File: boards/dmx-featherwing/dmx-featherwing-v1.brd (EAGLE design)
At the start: 50.8 x 22.9 mm, 4 parts, among them U2 MAX3468CSA

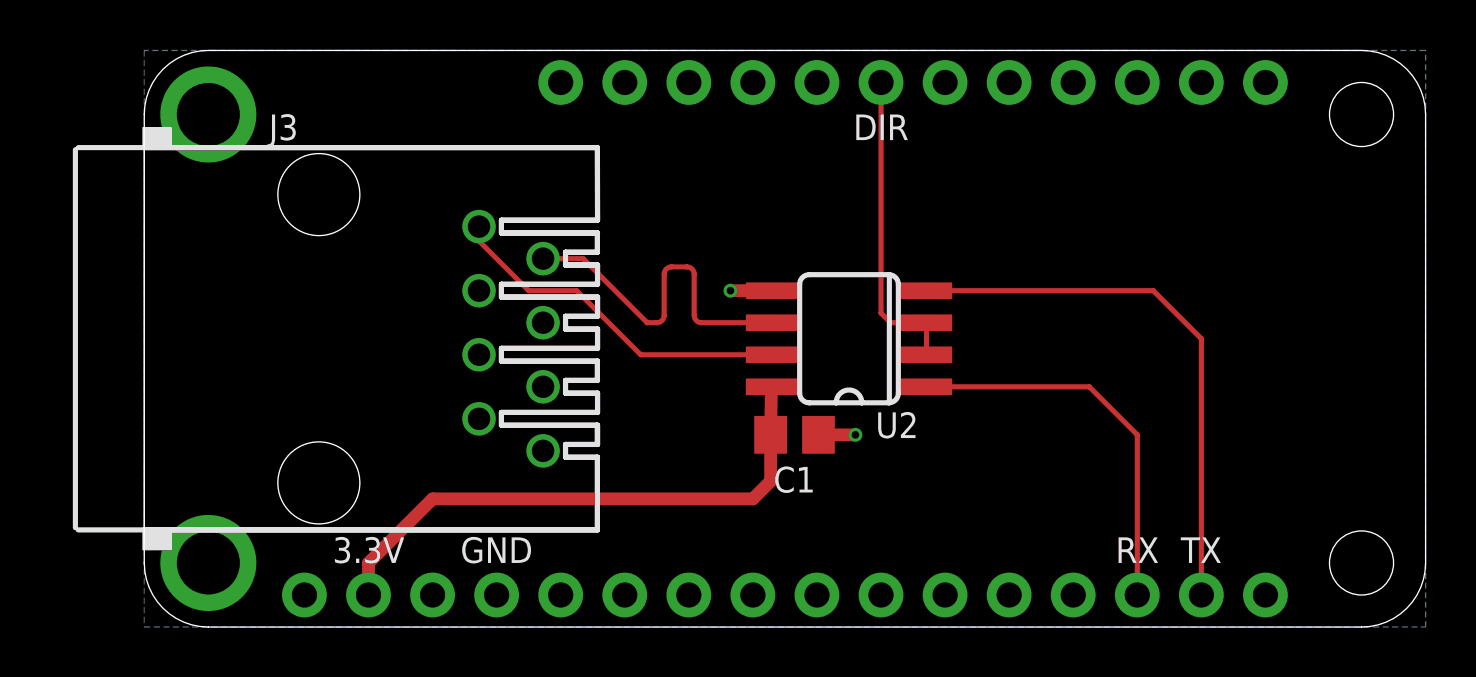
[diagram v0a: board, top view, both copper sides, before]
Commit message: Added termination resistor, ESD protection, and chassis ground.
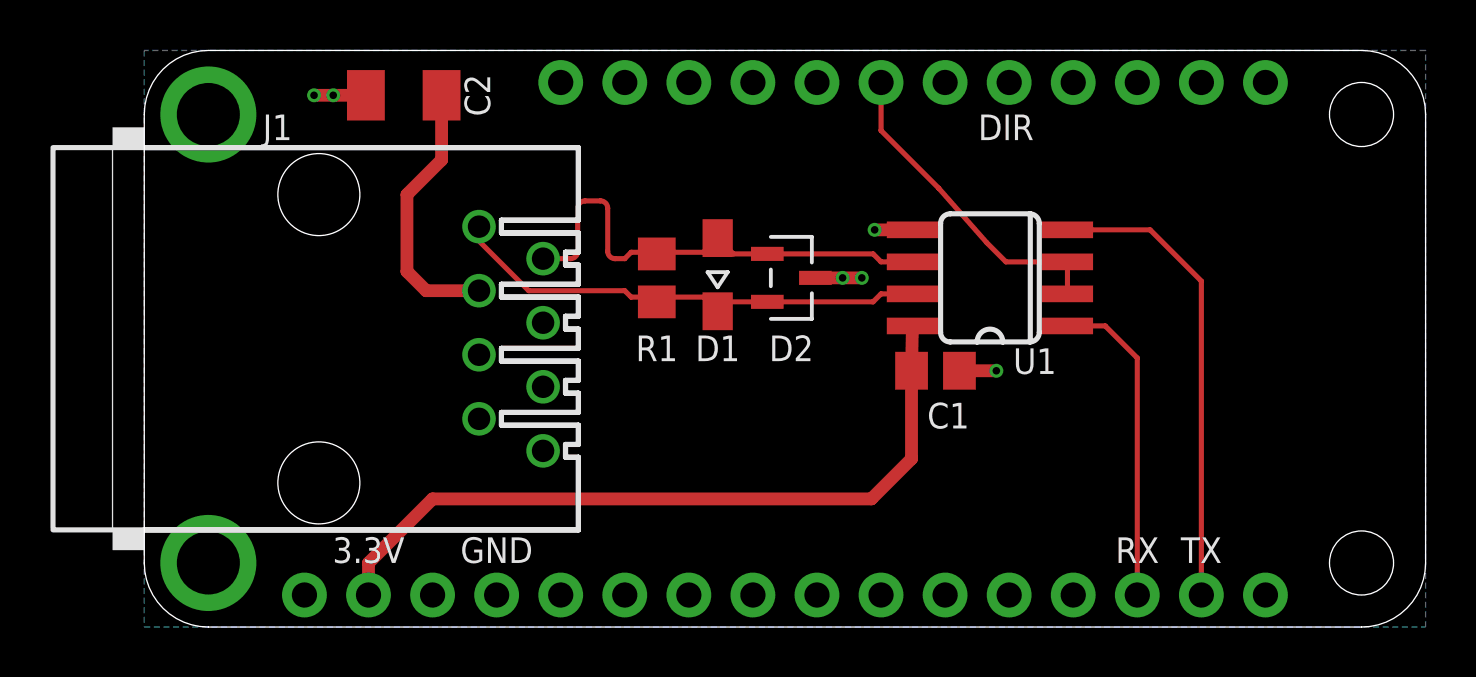
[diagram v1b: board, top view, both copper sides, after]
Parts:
- removed J3: (no value), con-amp:520251-4
- removed U2: MAX3468CSA, maxim:SO08
- added 120: (no value), rcl:R0805
- added C2: 1000pF 2kV, rcl:C1206K
- added D1: CDSOD323-T12SC, diode:SOD323-W
- added D2: CDSOT23-SM712, CDSOT23-SM712:SOT_SM712
- added J1: 5520251-4, TE 5520251-4:5520251-4
- added U1: SN65HVD11D, maxim:SO08
- C1: value (none) -> 0.1uF 10V X7R
- moved C1 6.14 mm to (31.4, 10.2)
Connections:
- new net N$1: C2.1, J1.3
- net +3V3: now also U1.8; no longer U2.8
- net D+: now also 120.1, D1.A, D2.1, J1.2, U1.6; no longer J3.2, U2.6
- net D-: now also 120.2, D1.C, D2.2, J1.1, U1.7; no longer J3.1, U2.7
- net DIR: now also U1.2, U1.3; no longer U2.2, U2.3
- net GND: now also C2.2, D2.3, U1.5; no longer U2.5
- net RXD: now also U1.1; no longer U2.1
- net TXD: now also U1.4; no longer U2.4
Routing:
- net N$1: track 0.00 -> 10.7 mm
- net +3V3: track 22.3 -> 29.8 mm
- net D+: track 13.9 -> 19.3 mm
- net D-: track 14.0 -> 19.4 mm
- net GND: track 3.09 -> 6.86 mm, vias 2 -> 6
- net TXD: track 21.8 -> 18.6 mm
- net RXD: track 15.5 -> 12.7 mm
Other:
- board text added: "C2"
- board text added: "D1"
- board text added: "D2"
- board text added: "J1"
- board text added: "R1"
- board text added: "U1"
- board text removed: "J3"
- board text removed: "U2"
